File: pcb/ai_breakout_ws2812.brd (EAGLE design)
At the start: 14 x 9.5 mm, 4 parts, among them J1 1X03, J2 1X03

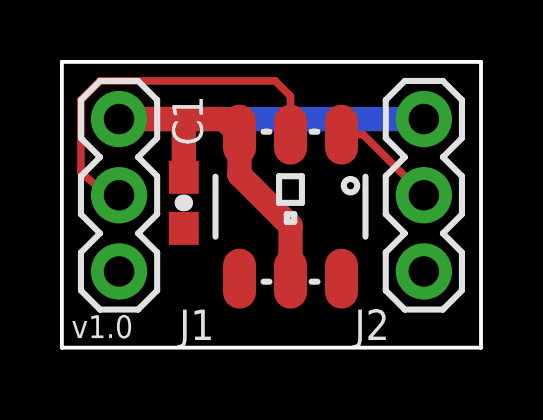
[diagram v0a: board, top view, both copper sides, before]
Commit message: Modified silkscreen on the board.
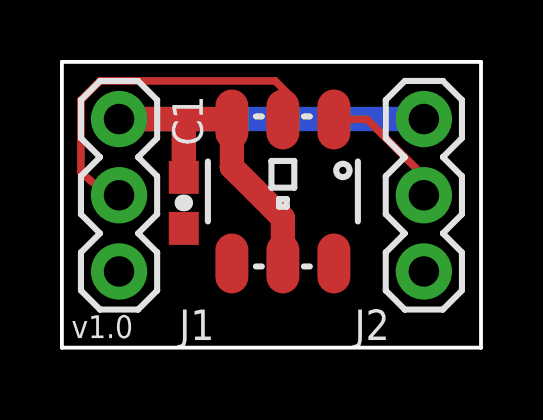
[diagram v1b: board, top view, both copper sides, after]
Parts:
- moved RGB 0.57 mm to (7.37, 5.21)
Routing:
- net DO: track 3.58 -> 4.42 mm

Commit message: Corrected silkscreen widths, BOM, searchable PDF schematic.
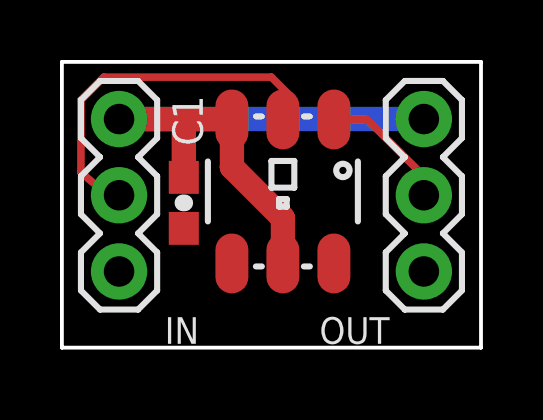
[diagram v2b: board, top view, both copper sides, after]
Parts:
- added U$5: AI-LOGOL, Ai_Miscellany:AI-LOGO-L
- renumbered J1 to IN, J2 to OUT
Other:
- board text added: "WS2812 Breakout"
- board text added: "http://acrobotic.com"
- board text removed: "/home/xisco/ai_logo.bmp"
- board text removed: "Ai WS2812 Breakout"

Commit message: Minor modifications.  Version is now 1.1.
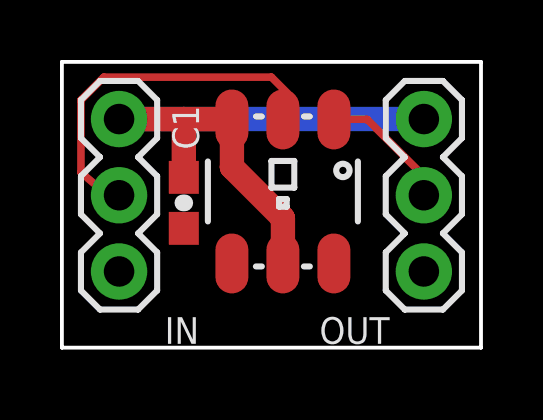
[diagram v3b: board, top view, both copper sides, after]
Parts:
- C1: device Ai_Passives:0603-CAP -> Ai_Passives:CAP-0603
- moved U$5 0.38 mm to (6.99, 5.08)
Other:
- board text added: "v1.1"
- board text removed: "v1.0"
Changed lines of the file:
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@@
 <wire x1="13.97" y1="9.525" x2="0" y2="9.525" width="0.127" layer="20"/>
 <wire x1="0" y1="9.525" x2="0" y2="0" width="0.127" layer="20"/>
-<text x="9.906" y="0.127" size="0.889" layer="22" font="vector" ratio="15" rot="SMR0"> WS2812
+<text x="9.906" y="0.254" size="0.889" layer="22" font="vector" ratio="15" rot="SMR0"> WS2812
 Breakout</text>
-<text x="2.667" y="0.254" size="0.762" layer="22" font="vector" ratio="15" rot="MR0">v1.0</text>
+<text x="2.667" y="0.254" size="0.762" layer="22" font="vector" ratio="15" rot="MR0">v1.1</text>
 <text x="3.937" y="5.715" size="0.889" layer="22" font="vector" ratio="15" rot="MR270">DI</text>
 <text x="3.937" y="8.89" size="0.889" layer="22" font="vector" ratio="15" rot="MR270">VCC</text>
@@
 <elements>
 <element name="RGB" library="Ai_LED" package="LED-WS2812" value="LED-WS2812" x="7.366" y="5.207" smashed="yes" rot="R270"/>
-<element name="C1" library="Ai_Passives" package="0603-CAP" value="0.1uF" x="4.064" y="4.826" smashed="yes" rot="R270">
-<attribute name="NAME" x="4.699" y="6.731" size="1.016" layer="25" font="vector" ratio="15" rot="R90"/>
+<element name="C1" library="Ai_Passives" package="CAP-0603" value="0.1uF" x="4.064" y="4.826" smashed="yes" rot="R270">
+<attribute name="NAME" x="4.572" y="6.604" size="0.889" layer="25" font="vector" ratio="15" rot="R90"/>
 </element>
 <element name="IN" library="Ai_Connectors" package="1X03" value="1X03" x="1.905" y="5.08" smashed="yes" rot="R90">
@@
 <attribute name="NAME" x="10.922" y="1.016" size="0.889" layer="25" font="vector" ratio="15" rot="R180"/>
 </element>
-<element name="U$5" library="Ai_Miscellany" package="AI-LOGO-L" value="AI-LOGOL" x="6.985" y="4.699" rot="MR0"/>
+<element name="U$5" library="Ai_Miscellany" package="AI-LOGO-L" value="AI-LOGOL" x="6.985" y="5.08" rot="MR0"/>
 </elements>
 <signals>
@@
 <signal name="DO">
 <contactref element="RGB" pad="1"/>
-<contactref element="OUT" pad="2"/>
 <wire x1="9.066" y1="7.607" x2="10.173" y2="7.607" width="0.254" layer="1"/>
 <wire x1="10.173" y1="7.607" x2="12.065" y2="5.715" width="0.254" layer="1"/>
+<contactref element="OUT" pad="2"/>
 <wire x1="12.065" y1="5.715" x2="12.065" y2="5.08" width="0.254" layer="1"/>
 </signal>

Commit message: Centered pins.
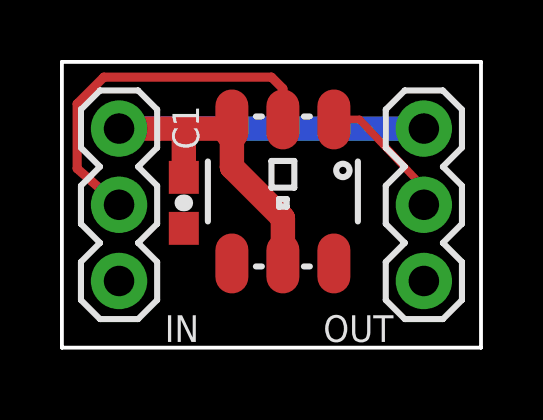
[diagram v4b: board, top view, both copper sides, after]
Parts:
- moved IN 0.32 mm to (1.91, 4.76)
- moved OUT 0.32 mm to (12.1, 4.76)
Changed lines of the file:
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@@
 <text x="9.906" y="0.254" size="0.889" layer="22" font="vector" ratio="15" rot="SMR0"> WS2812
 Breakout</text>
-<text x="2.667" y="0.254" size="0.762" layer="22" font="vector" ratio="15" rot="MR0">v1.1</text>
-<text x="3.937" y="5.715" size="0.889" layer="22" font="vector" ratio="15" rot="MR270">DI</text>
-<text x="3.937" y="8.89" size="0.889" layer="22" font="vector" ratio="15" rot="MR270">VCC</text>
-<text x="3.937" y="3.683" size="0.889" layer="22" font="vector" ratio="15" rot="MR270">GND</text>
-<text x="10.922" y="3.683" size="0.889" layer="22" font="vector" ratio="15" rot="MR270">GND</text>
-<text x="10.922" y="5.969" size="0.889" layer="22" font="vector" ratio="15" rot="MR270">DO</text>
-<text x="10.922" y="8.89" size="0.889" layer="22" font="vector" ratio="15" rot="MR270">VCC</text>
-<text x="10.922" y="8.89" size="0.508" layer="22" font="vector" ratio="15" rot="MR0">http://acrobotic.com</text>
+<text x="2.159" y="0.127" size="0.635" layer="22" font="vector" ratio="15" rot="MR0">v1.1</text>
+<text x="3.937" y="5.461" size="0.889" layer="22" font="vector" ratio="15" rot="MR270">DI</text>
+<text x="3.937" y="8.636" size="0.889" layer="22" font="vector" ratio="15" rot="MR270">VCC</text>
+<text x="3.937" y="3.429" size="0.889" layer="22" font="vector" ratio="15" rot="MR270">GND</text>
+<text x="10.922" y="3.429" size="0.889" layer="22" font="vector" ratio="15" rot="MR270">GND</text>
+<text x="10.922" y="5.715" size="0.889" layer="22" font="vector" ratio="15" rot="MR270">DO</text>
+<text x="10.922" y="8.636" size="0.889" layer="22" font="vector" ratio="15" rot="MR270">VCC</text>
+<text x="10.922" y="8.636" size="0.508" layer="22" font="vector" ratio="15" rot="MR0">http://acrobotic.com</text>
 </plain>
 <attributes>
@@
 <attribute name="NAME" x="4.572" y="6.604" size="0.889" layer="25" font="vector" ratio="15" rot="R90"/>
 </element>
-<element name="IN" library="Ai_Connectors" package="1X03" value="1X03" x="1.905" y="5.08" smashed="yes" rot="R90">
-<attribute name="NAME" x="4.572" y="1.016" size="0.889" layer="25" font="vector" ratio="15" rot="R180"/>
+<element name="IN" library="Ai_Connectors" package="1X03" value="1X03" x="1.905" y="4.7625" smashed="yes" rot="R90">
+<attribute name="NAME" x="4.572" y="1.0795" size="0.889" layer="25" font="vector" ratio="15" rot="R180"/>
 </element>
-<element name="OUT" library="Ai_Connectors" package="1X03" value="1X03" x="12.065" y="5.08" smashed="yes" rot="R90">
-<attribute name="NAME" x="10.922" y="1.016" size="0.889" layer="25" font="vector" ratio="15" rot="R180"/>
+<element name="OUT" library="Ai_Connectors" package="1X03" value="1X03" x="12.065" y="4.7625" smashed="yes" rot="R90">
+<attribute name="NAME" x="11.049" y="1.0795" size="0.889" layer="25" font="vector" ratio="15" rot="R180"/>
 </element>
 <element name="U$5" library="Ai_Miscellany" package="AI-LOGO-L" value="AI-LOGOL" x="6.985" y="5.08" rot="MR0"/>
@@
 <contactref element="OUT" pad="3"/>
 <contactref element="IN" pad="3"/>
-<wire x1="1.905" y1="7.62" x2="4.064" y2="7.62" width="0.8128" layer="1"/>
-<wire x1="4.064" y1="7.62" x2="5.399" y2="7.62" width="0.8128" layer="1"/>
-<wire x1="5.399" y1="7.62" x2="5.666" y2="7.607" width="0.8128" layer="1"/>
+<wire x1="1.905" y1="7.3025" x2="4.064" y2="7.3025" width="0.8128" layer="1"/>
+<wire x1="4.064" y1="7.3025" x2="5.399" y2="7.3025" width="0.8128" layer="1"/>
+<wire x1="5.399" y1="7.3025" x2="5.666" y2="7.607" width="0.8128" layer="1"/>
 <wire x1="5.666" y1="7.607" x2="5.666" y2="6.018" width="0.8128" layer="1"/>
 <wire x1="5.666" y1="6.018" x2="7.366" y2="4.318" width="0.8128" layer="1"/>
 <wire x1="7.366" y1="4.318" x2="7.366" y2="2.807" width="0.8128" layer="1"/>
-<wire x1="4.064" y1="5.676" x2="4.064" y2="7.62" width="0.8128" layer="1"/>
-<wire x1="12.065" y1="7.62" x2="1.905" y2="7.62" width="0.8128" layer="16"/>
+<wire x1="4.064" y1="5.676" x2="4.064" y2="7.3025" width="0.8128" layer="1"/>
+<wire x1="12.065" y1="7.3025" x2="1.905" y2="7.3025" width="0.8128" layer="16"/>
 </signal>
 <signal name="GND">
@@
 <contactref element="RGB" pad="2"/>
 <contactref element="IN" pad="2"/>
-<wire x1="1.905" y1="5.08" x2="1.524" y2="5.08" width="0.254" layer="1"/>
-<wire x1="1.524" y1="5.08" x2="0.635" y2="5.842" width="0.254" layer="1"/>
-<wire x1="0.635" y1="5.842" x2="0.635" y2="8.255" width="0.254" layer="1"/>
-<wire x1="0.635" y1="8.255" x2="1.397" y2="9.017" width="0.254" layer="1"/>
-<wire x1="1.397" y1="9.017" x2="6.985" y2="9.017" width="0.254" layer="1"/>
-<wire x1="6.985" y1="9.017" x2="7.62" y2="8.382" width="0.254" layer="1"/>
-<wire x1="7.62" y1="8.382" x2="7.366" y2="7.607" width="0.254" layer="1"/>
+<wire x1="1.905" y1="4.7625" x2="1.524" y2="5.08" width="0.3048" layer="1"/>
+<wire x1="1.524" y1="5.08" x2="0.508" y2="5.969" width="0.3048" layer="1"/>
+<wire x1="0.508" y1="5.969" x2="0.508" y2="8.128" width="0.3048" layer="1"/>
+<wire x1="0.508" y1="8.128" x2="1.397" y2="9.017" width="0.3048" layer="1"/>
+<wire x1="1.397" y1="9.017" x2="6.985" y2="9.017" width="0.3048" layer="1"/>
+<wire x1="6.985" y1="9.017" x2="7.366" y2="8.636" width="0.3048" layer="1"/>
+<wire x1="7.366" y1="8.636" x2="7.366" y2="7.607" width="0.3048" layer="1"/>
 </signal>
 <signal name="DO">
 <contactref element="RGB" pad="1"/>
-<wire x1="9.066" y1="7.607" x2="10.173" y2="7.607" width="0.254" layer="1"/>
-<wire x1="10.173" y1="7.607" x2="12.065" y2="5.715" width="0.254" layer="1"/>
+<wire x1="9.066" y1="7.607" x2="9.919" y2="7.607" width="0.254" layer="1"/>
+<wire x1="9.919" y1="7.607" x2="12.065" y2="5.334" width="0.254" layer="1"/>
 <contactref element="OUT" pad="2"/>
-<wire x1="12.065" y1="5.715" x2="12.065" y2="5.08" width="0.254" layer="1"/>
+<wire x1="12.065" y1="5.334" x2="12.065" y2="4.7625" width="0.254" layer="1"/>
 </signal>
 </signals>
